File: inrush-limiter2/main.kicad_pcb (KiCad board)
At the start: 2 copper layers, 32 parts, among them K1 RELAY_2RT, P1 CONN_01X04, P2 CONN_01X02, Q1 2N3904, Q2 PN2222A, T1 MY-TRANSFO, U1 LM393, U2 50 ohm NTC

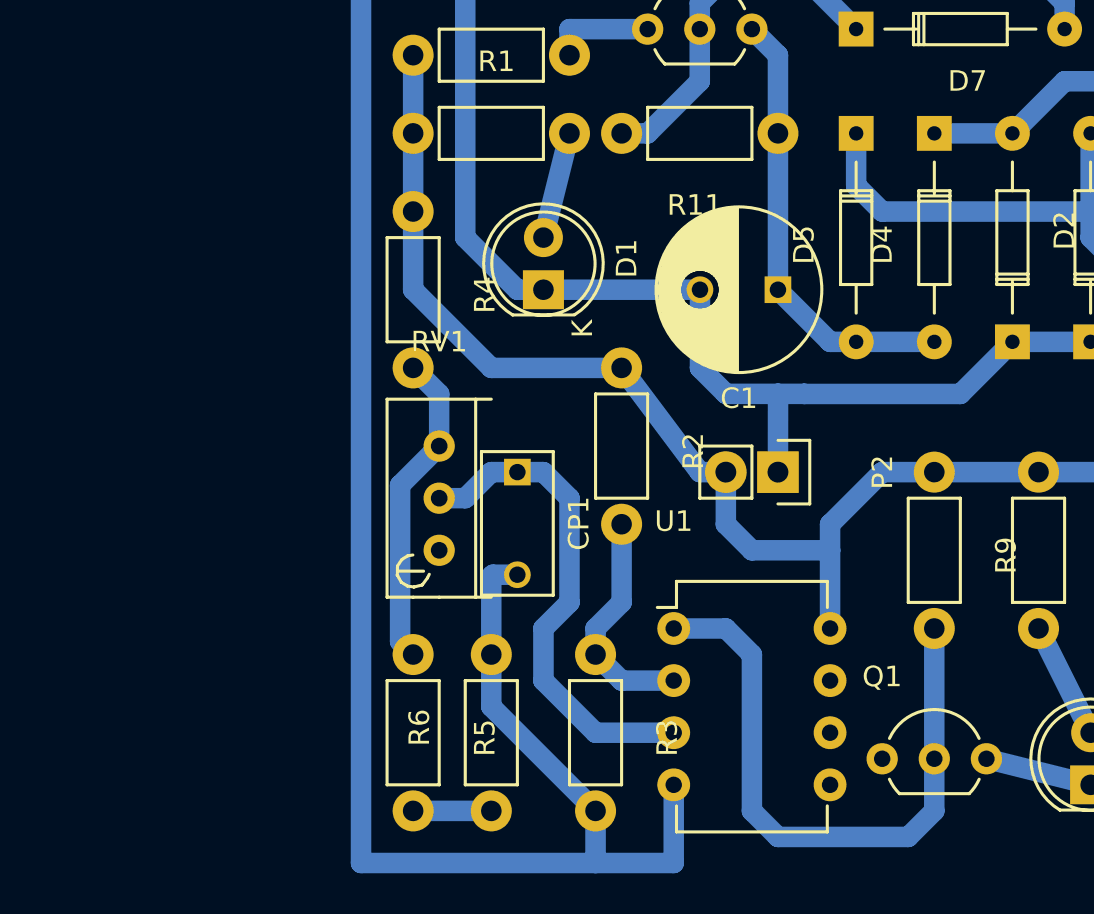
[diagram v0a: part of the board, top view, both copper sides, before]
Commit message: update, problem with transistor to ground
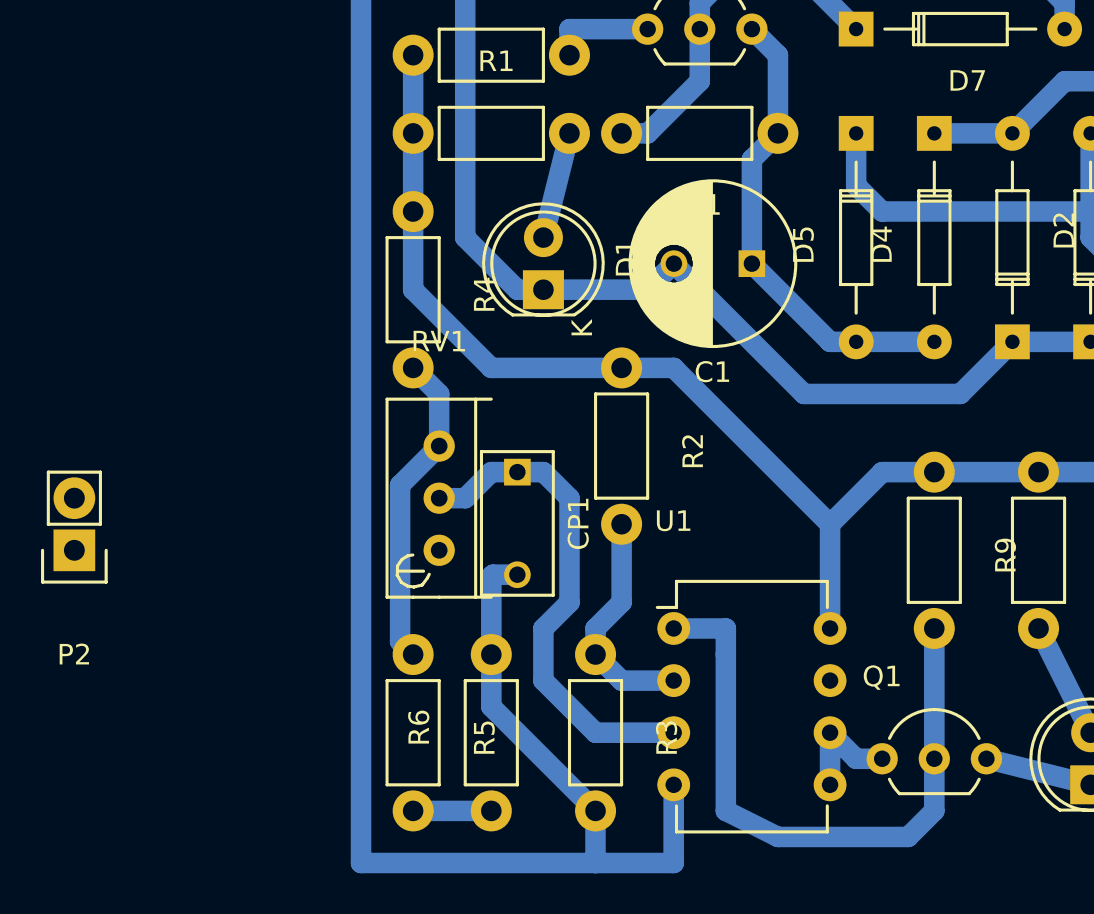
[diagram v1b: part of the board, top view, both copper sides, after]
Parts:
- moved P2 34.5 mm to (100.3, 80.0), turned to 180 degrees
- moved C1 1.80 mm to (133.3, 66.0)
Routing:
- net +5V: track 112.5 -> 110.0 mm
- net Net-(C1-Pad1): track 21.9 -> 23.0 mm
- net GND: track 172.4 -> 173.0 mm
- net Net-(Q1-Pad2): track 30.8 -> 31.3 mm
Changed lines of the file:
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@@
     (links 58)
     (no_connects 4)
-    (area 110.105 47.685 234.358001 96.28099)
+    (area 93.421667 47.685 234.358001 96.28099)
     (thickness 1.6)
     (drawings 0)
-    (tracks 175)
+    (tracks 173)
     (zones 0)
     (modules 32)
@@
   )
   (module Capacitors_ThroughHole:C_Radial_D8_L13_P3.8 (layer F.Cu)
-    (at 134.62 67.31 180)
+    (at 133.35 66.04 180)
     (descr "Radial Electrolytic Capacitor Diameter 8mm x Length 13mm, Pitch 3.8mm")
     (tags "Electrolytic Capacitor")
@@
   )
   (module Pin_Headers:Pin_Header_Straight_1x02 (layer F.Cu)
-    (at 134.62 76.2 270)
+    (at 100.33 80.01 180)
     (descr "Through hole pin header")
     (tags "pin header")
-    (fp_text reference P2 (at 0 -5.1 270) (layer F.SilkS)
-      (effects (font (size 1 1) (thickness 0.15)))
-    )
-    (fp_text value CONN_01X02 (at 0 -3.1 270) (layer F.Fab)
+    (fp_text reference P2 (at 0 -5.1 180) (layer F.SilkS)
+      (effects (font (size 1 1) (thickness 0.15)))
+    )
+    (fp_text value CONN_01X02 (at 0 -3.1 180) (layer F.Fab)
       (effects (font (size 1 1) (thickness 0.15)))
     )
@@
     (fp_line (start -1.27 1.27) (end -1.27 3.81) (layer F.SilkS) (width 0.15))
     (fp_line (start -1.27 3.81) (end 1.27 3.81) (layer F.SilkS) (width 0.15))
-    (pad 1 thru_hole rect (at 0 0 270) (size 2.032 2.032) (drill 1.016) (layers *.Cu *.Mask F.SilkS)
+    (pad 1 thru_hole rect (at 0 0 180) (size 2.032 2.032) (drill 1.016) (layers *.Cu *.Mask F.SilkS)
       (net 2 GND))
-    (pad 2 thru_hole oval (at 0 2.54 270) (size 2.032 2.032) (drill 1.016) (layers *.Cu *.Mask F.SilkS)
+    (pad 2 thru_hole oval (at 0 2.54 180) (size 2.032 2.032) (drill 1.016) (layers *.Cu *.Mask F.SilkS)
       (net 22 +5V))
     (model Pin_Headers.3dshapes/Pin_Header_Straight_1x02.wrl
@@
     (pad 10 thru_hole circle (at 9.99998 9.99998 180) (size 2.99974 2.99974) (drill 1.50114) (layers *.Cu *.Mask F.SilkS))
   )
+  (segment (start 138.43254 69.85052) (end 137.16052 69.85052) (width 1) (layer B.Cu) (net 1) (status 400000))
+  (segment (start 137.16052 69.85052) (end 133.35 66.04) (width 1) (layer B.Cu) (net 1) (status 800000))
+  (segment (start 133.35 66.04) (end 133.35 60.96) (width 1) (layer B.Cu) (net 1) (status 400000))
+  (segment (start 133.35 60.96) (end 134.62 59.69) (width 1) (layer B.Cu) (net 1) (status 800000))
   (segment (start 133.35 54.61) (end 134.62 55.88) (width 1) (layer B.Cu) (net 1) (status 10))
   (segment (start 134.62 55.88) (end 134.62 59.69) (width 1) (layer B.Cu) (net 1) (status 20))
-  (segment (start 134.62 59.69) (end 134.62 67.31) (width 1) (layer B.Cu) (net 1) (status 30))
-  (segment (start 138.43254 69.85052) (end 137.16052 69.85052) (width 1) (layer B.Cu) (net 1) (status 10))
-  (segment (start 137.16052 69.85052) (end 134.62 67.31) (width 1) (layer B.Cu) (net 1) (status 20))
   (segment (start 138.43254 69.85052) (end 142.24254 69.85052) (width 1) (layer B.Cu) (net 1) (status 30))
-  (segment (start 134.62052 67.30948) (end 134.62 67.31) (width 1) (layer B.Cu) (net 1) (status 30))
+  (segment (start 133.35052 66.03948) (end 133.35 66.04) (width 1) (layer B.Cu) (net 1) (status 30))
   (segment (start 142.24254 69.85052) (end 142.23948 69.85052) (width 1) (layer B.Cu) (net 1) (status 30))
   (segment (start 133.35 54.61104) (end 133.35 54.61) (width 1) (layer B.Cu) (net 1) (status 30))
   (segment (start 142.24202 69.85) (end 142.24254 69.85052) (width 1) (layer B.Cu) (net 1) (status 30))
   (segment (start 138.43 69.84798) (end 138.43254 69.85052) (width 1) (layer B.Cu) (net 1) (status 30))
+  (segment (start 146.04746 69.84948) (end 146.04746 69.85254) (width 1) (layer B.Cu) (net 2) (status C00000))
+  (segment (start 146.04746 69.85254) (end 143.51 72.39) (width 1) (layer B.Cu) (net 2) (status 400000))
+  (segment (start 135.89 72.39) (end 129.55 66.05) (width 1) (layer B.Cu) (net 2) (status 800000))
+  (segment (start 143.51 72.39) (end 135.89 72.39) (width 1) (layer B.Cu) (net 2))
+  (segment (start 129.55 66.05) (end 129.55 66.04) (width 1) (layer B.Cu) (net 2) (status C00000))
+  (segment (start 123.19 67.31) (end 128.27 67.31) (width 1) (layer B.Cu) (net 2) (status 400000))
+  (segment (start 128.27 67.31) (end 129.54 66.04) (width 1) (layer B.Cu) (net 2) (status 800000))
+  (segment (start 129.54 66.04) (end 129.55 66.04) (width 1) (layer B.Cu) (net 2) (status C00000))
+  (segment (start 137.16 88.9) (end 138.43 90.17) (width 1) (layer B.Cu) (net 2) (status 10))
+  (segment (start 138.43 90.17) (end 139.7 90.17) (width 1) (layer B.Cu) (net 2) (status 20))
+  (segment (start 137.16 88.9) (end 137.16 91.44) (width 1) (layer B.Cu) (net 2) (status 30))
   (segment (start 121.92 81.2) (end 120.73 81.2) (width 1) (layer B.Cu) (net 2) (status 10))
   (segment (start 120.65 81.28) (end 120.65 85.09) (width 1) (layer B.Cu) (net 2) (status 20))
@@
   (segment (start 114.3 50.8) (end 114.3 95.25) (width 1) (layer B.Cu) (net 2))
   (segment (start 121.92 81.2) (end 121.92 81.28) (width 1) (layer B.Cu) (net 2) (status 30))
-  (segment (start 134.625 72.385) (end 132.085 72.385) (width 1) (layer B.Cu) (net 2))
-  (segment (start 130.82 71.12) (end 130.82 67.31) (width 1) (layer B.Cu) (net 2) (status 20))
-  (segment (start 132.085 72.385) (end 130.82 71.12) (width 1) (layer B.Cu) (net 2))
-  (segment (start 135.895 72.385) (end 134.625 72.385) (width 1) (layer B.Cu) (net 2))
-  (segment (start 134.625 72.385) (end 134.62 76.2) (width 1) (layer B.Cu) (net 2) (status 20))
   (segment (start 120.65 85.09) (end 120.65 87.63) (width 1) (layer B.Cu) (net 2) (status 10))
   (segment (start 120.65 87.63) (end 125.73 92.71) (width 1) (layer B.Cu) (net 2) (status 20))
@@
   (segment (start 129.54 95.25) (end 125.73 95.25) (width 1) (layer B.Cu) (net 2))
   (segment (start 139.69746 90.17254) (end 139.7 90.17) (width 1) (layer B.Cu) (net 2) (status 30))
-  (segment (start 146.04746 69.84948) (end 146.04746 69.85254) (width 1) (layer B.Cu) (net 2) (status 30))
-  (segment (start 146.04746 69.85254) (end 143.51 72.39) (width 1) (layer B.Cu) (net 2) (status 10))
-  (segment (start 135.9 72.39) (end 135.895 72.385) (width 1) (layer B.Cu) (net 2))
-  (segment (start 143.51 72.39) (end 135.9 72.39) (width 1) (layer B.Cu) (net 2))
-  (segment (start 130.82 67.31) (end 123.19 67.31) (width 1) (layer B.Cu) (net 2) (status 30))
   (segment (start 149.86 69.85202) (end 149.85746 69.84948) (width 1) (layer B.Cu) (net 2) (status 30))
   (segment (start 149.85746 69.84948) (end 146.04746 69.84948) (width 1) (layer B.Cu) (net 2) (status 30))
@@
   (segment (start 134.62 93.98) (end 140.97 93.98) (width 1) (layer B.Cu) (net 7))
   (segment (start 132.08 83.82) (end 129.54 83.82) (width 1) (layer B.Cu) (net 7) (status 20))
-  (segment (start 132.08 83.82) (end 133.35 85.09) (width 1) (layer B.Cu) (net 7))
-  (segment (start 133.35 85.09) (end 133.35 92.71) (width 1) (layer B.Cu) (net 7))
-  (segment (start 133.35 92.71) (end 134.62 93.98) (width 1) (layer B.Cu) (net 7))
+  (segment (start 132.08 83.82) (end 132.08 85.09) (width 1) (layer B.Cu) (net 7))
+  (segment (start 132.08 85.09) (end 132.08 92.71) (width 1) (layer B.Cu) (net 7))
+  (segment (start 132.08 92.71) (end 134.62 93.98) (width 1) (layer B.Cu) (net 7))
   (segment (start 140.97 93.98) (end 142.24 92.71) (width 1) (layer B.Cu) (net 7))
   (segment (start 142.24 90.17) (end 142.24 92.71) (width 1) (layer B.Cu) (net 7) (status 10))
@@
   (segment (start 119.38 77.47) (end 118.11 77.47) (width 1) (layer B.Cu) (net 21) (status 20))
   (segment (start 120.65 76.2) (end 119.38 77.47) (width 1) (layer B.Cu) (net 21))
+  (segment (start 127 71.12) (end 129.54 71.12) (width 1) (layer B.Cu) (net 22))
+  (segment (start 129.54 71.12) (end 137.16 78.74) (width 1) (layer B.Cu) (net 22))
   (segment (start 193.04 91.44) (end 190.5 88.9) (width 1) (layer B.Cu) (net 22) (status 10))
   (segment (start 152.4 86.36) (end 152.4 77.47) (width 1) (layer B.Cu) (net 22))
@@
   (segment (start 120.65 71.12) (end 116.84 67.31) (width 1) (layer B.Cu) (net 22))
   (segment (start 142.24 76.2) (end 139.7 76.2) (width 1) (layer B.Cu) (net 22) (status 10))
-  (segment (start 137.16 78.74) (end 137.16 80.01) (width 1) (layer B.Cu) (net 22))
   (segment (start 139.7 76.2) (end 137.16 78.74) (width 1) (layer B.Cu) (net 22))
-  (segment (start 132.08 76.2) (end 132.08 78.74) (width 1) (layer B.Cu) (net 22) (status 10))
-  (segment (start 132.08 78.74) (end 133.35 80.01) (width 1) (layer B.Cu) (net 22))
-  (segment (start 133.35 80.01) (end 137.16 80.01) (width 1) (layer B.Cu) (net 22))
-  (segment (start 130.81 76.2) (end 132.08 76.2) (width 1) (layer B.Cu) (net 22) (status 20))
-  (segment (start 130.81 76.2) (end 127 71.12) (width 1) (layer B.Cu) (net 22) (status 20))
+  (segment (start 137.16 78.74) (end 137.16 83.82) (width 1) (layer B.Cu) (net 22) (status 20))
   (segment (start 116.84 63.5) (end 116.84 59.69) (width 1) (layer B.Cu) (net 22) (status 30))
   (segment (start 116.84 59.69) (end 116.84 55.88) (width 1) (layer B.Cu) (net 22) (status 30))
-  (segment (start 137.16 80.01) (end 137.16 83.82) (width 1) (layer B.Cu) (net 22) (status 20))
   (segment (start 147.32 76.2) (end 142.24 76.2) (width 1) (layer B.Cu) (net 22) (status 30))
   (segment (start 218.821 87.122) (end 212.852 87.122) (width 2.5) (layer B.Cu) (net 23) (status 10))

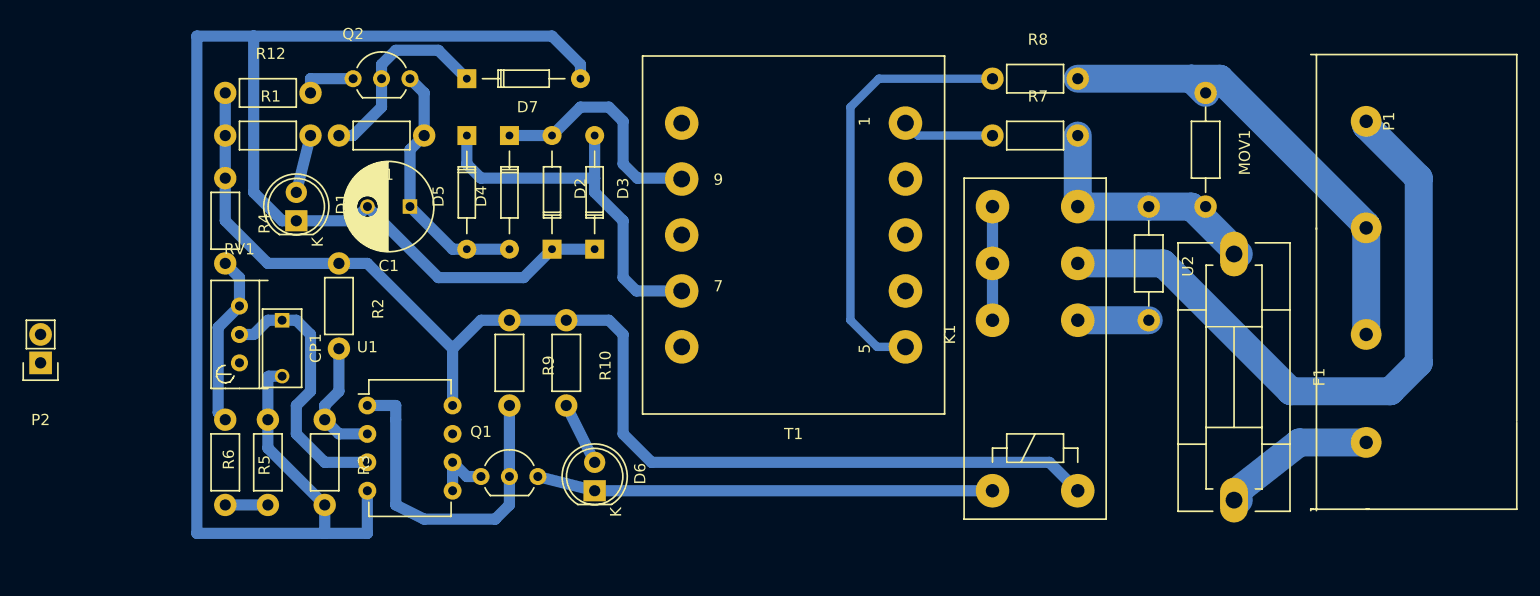
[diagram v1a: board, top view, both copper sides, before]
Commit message: fixed with a resistor but not sure its necessary
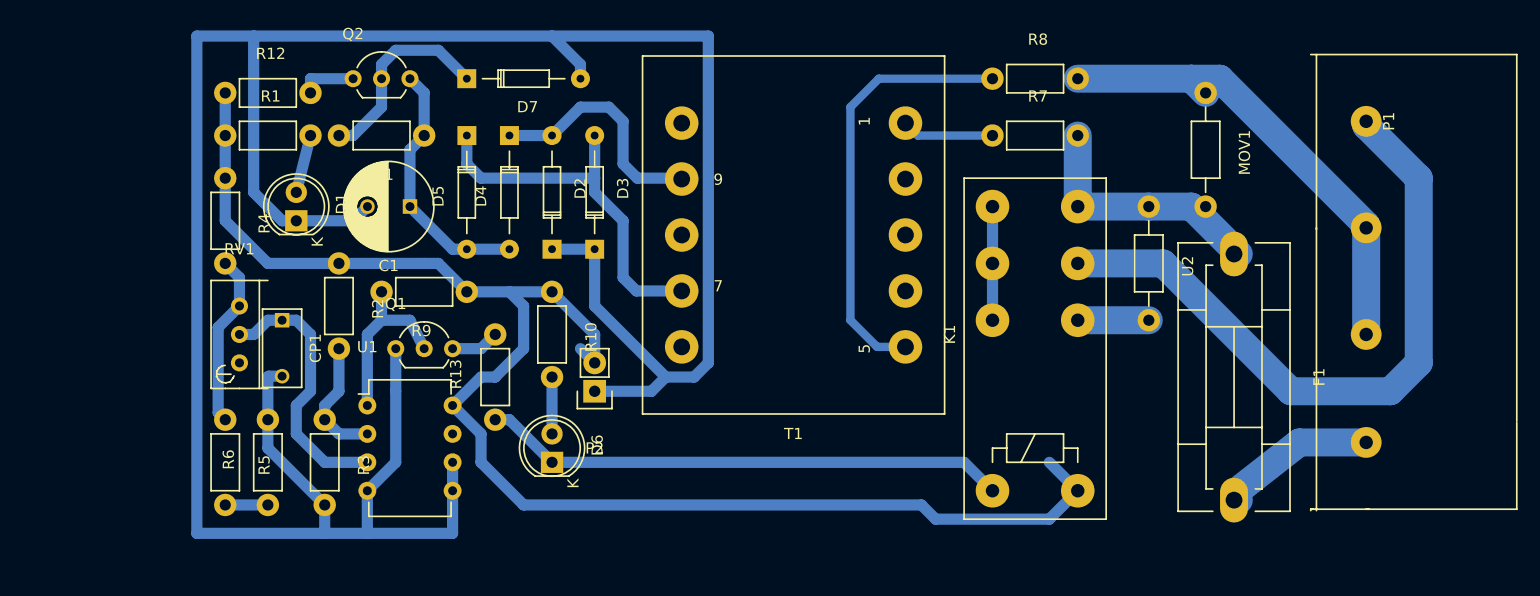
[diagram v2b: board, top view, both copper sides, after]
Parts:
- added R13: 0, Resistors_ThroughHole:Resistor_Horizontal_RM7mm, F.Cu at (141.0, 85.1)
- moved P2 49.6 mm to (149.9, 82.5)
- moved Q1 13.7 mm to (132.1, 78.7)
- moved R9 4.58 mm to (138.4, 73.7), turned to 180 degrees
- moved D6 4.58 mm to (146.1, 88.9)
- moved R10 2.84 mm to (146.1, 73.7)
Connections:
- Q1 pad 3: Net-(D6-Pad1) -> Net-(Q1-Pad3)
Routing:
- net GND: track 173.0 -> 243.4 mm
- net +5V: track 110.0 -> 133.3 mm
- net Net-(Q1-Pad2): track 31.3 -> 16.1 mm
- net Net-(D6-Pad1): track 40.8 -> 47.1 mm
- net Net-(Q1-Pad3): track 0.00 -> 4.34 mm
- net Net-(D6-Pad2): track 5.68 -> 5.08 mm

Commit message: yes its needed
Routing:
- net AC-live-f: track 23.2 -> 23.9 mm
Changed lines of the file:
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@@
   (general
     (links 59)
-    (no_connects 1)
-    (area -3.275001 -6.42512 234.358001 96.28099)
+    (no_connects 0)
+    (area 110.105 47.685 234.358001 96.28099)
     (thickness 1.6)
     (drawings 0)
@@
   (segment (start 123.19254 67.31052) (end 123.19 67.30798) (width 1) (layer B.Cu) (net 2) (status 30))
   (segment (start 146.04798 69.85) (end 146.04746 69.84948) (width 1) (layer B.Cu) (net 2) (status 30))
+  (segment (start 207.01 70.27926) (end 207.01 68.58) (width 2.5) (layer B.Cu) (net 3) (status C00000))
+  (segment (start 207.01 68.58) (end 204.47 66.04) (width 2.5) (layer B.Cu) (net 3) (status C00000))
+  (segment (start 204.47 66.04) (end 199.39 66.04) (width 2.5) (layer B.Cu) (net 3) (status C00000))
   (segment (start 193.04 66.04) (end 193.04 59.69) (width 2.5) (layer B.Cu) (net 3) (status 30))
   (segment (start 207.01 70.27926) (end 207.01 69.85) (width 2.5) (layer B.Cu) (net 3) (status 30))
-  (segment (start 207.01 69.85) (end 203.2 66.04) (width 2.5) (layer B.Cu) (net 3) (status 10))
-  (segment (start 203.2 66.04) (end 199.39 66.04) (width 2.5) (layer B.Cu) (net 3) (status 20))
   (segment (start 207.01 70.27926) (end 207.01 69.85) (width 2.5) (layer B.Cu) (net 3) (status 30))
   (segment (start 199.39 66.04) (end 193.04 66.04) (width 2.5) (layer B.Cu) (net 3) (status 30))
-  (segment (start 207.01 70.27926) (end 207.43926 70.27926) (width 2.5) (layer B.Cu) (net 3) (status 30))
   (segment (start 157.56128 63.5) (end 153.67 63.5) (width 1) (layer B.Cu) (net 4) (status 10))
   (segment (start 151.13 57.15) (end 152.4 58.42) (width 1) (layer B.Cu) (net 4))

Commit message: tidy
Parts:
- moved P2 13.5 mm to (141.0, 92.7)
- moved D6 1.27 mm to (146.1, 87.6)
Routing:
- net +5V: track 133.3 -> 120.7 mm
- net Net-(D6-Pad1): track 47.1 -> 49.8 mm
- net Net-(D6-Pad2): track 5.08 -> 3.81 mm
- net GND: track 243.4 -> 242.2 mm
